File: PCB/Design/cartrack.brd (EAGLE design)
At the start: 100 x 80 mm, 37 parts, among them J1 POWER_JACKPTH, Q4 12MHz, Q5 LM2941, U1 ATMEGA644P-20AU

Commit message: Finished schematic.
Started on PCB.
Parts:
- removed J2: (no value), SparkFun-Connectors:JST-2-SMD
- removed JP1: USBSMD, SparkFun-Connectors:USB-MINIB
- removed U$3: SIMHOLDER, SparkFun-Connectors:SIMHOLDER
- added C10, C18: 1uF, SparkFun-Passives:CAP-PTH-SMALL
- added C12, C14, C19: 100nF, SparkFun-Passives:1206
- added C13, C6: (no value), SparkFun-Passives:0603-CAP
- added C15, C20: 10nF, SparkFun-Passives:0603-CAP
- added C7: 1mF, resistor:E3,5-8
- added C8, C9: 2.2uF, SparkFun-Passives:1206
- added L1, L2: (no value), resistor:L2012C
- added U$13: SIMHOLDER3, SparkFun-Connectors:SIMHOLDER3
- added X1: BU-SMA-V, con-coax:BU-SMA-V
- SJ1: value SOLDERJUMPERROUND -> SOLDERJUMPERNO; device SparkFun-Retired:SJ_ROUND -> SparkFun-Retired:SJ_2S-NO
- moved SPI 255.3 mm to (69.0, 19.0), turned to 270 degrees
- moved UARTS 246.6 mm to (46.0, 32.0), turned to 270 degrees
- moved JTAG 212.7 mm to (61.0, 51.0), turned to 90 degrees
- moved J1 206.5 mm to (48.0, -3.00)
- moved C5 203.5 mm to (37.0, 8.00), turned to 270 degrees
- moved C4 200.6 mm to (32.0, 16.0), turned to 90 degrees
- moved R13 184.8 mm to (35.4, 3.90), turned to 270 degrees
- moved R12 180.5 mm to (37.5, 3.90), turned to 270 degrees
- moved R11 177.1 mm to (43.5, 23.7), flipped to the bottom, turned to 270 degrees
- moved Q3 174.8 mm to (59.0, 43.0), flipped to the bottom
- moved S1 172.7 mm to (40.7, 17.6), turned to 270 degrees
- moved SJ1 172.3 mm to (60.0, 33.0), flipped to the bottom, turned to 180 degrees
- moved Q4 165.6 mm to (64.0, 10.0), flipped to the bottom
- moved R10 165.6 mm to (58.0, 39.0), flipped to the bottom, turned to 90 degrees
- moved R9 165.2 mm to (63.0, 41.0), flipped to the bottom, turned to 90 degrees
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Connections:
- new net ANT: C6.1, L2.1, U$1.RF_ANT
- new net N$14: C6.2, L1.1, X1.1
- net +2V8: now also C10.1, C12.1, C13.1, C14.1, C15.1
- net +4V: now also C18.1, C19.1, C20.1, C7.+, C8.1, C9.1
- net +5V: no longer J2.2, JP1.VBUS
- net 0V: now also C10.2, C12.2, C13.2, C14.2, C15.2, C18.2, C19.2, C20.2, C7.-, C8.2, C9.2, L1.2, L2.2, U$13.6, X1.2, X1.3, X1.4, X1.5; no longer J2.1, JP1.GND, U$3.C5
- net GSM_PWR: now also U$4.3
- net N$1: now also U$13.4, U$4.4; no longer U$3.C7, U$4.1
- net N$2: now also U$13.3, U$4.5; no longer U$3.C3, U$4.6
- net N$3: now also U$13.2, U$4.6; no longer U$3.C2, U$4.4
- net SIM_VDD: now also U$13.1, U$4.1; no longer U$3.C1, U$4.3
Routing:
- net +4V: track 0.00 -> 127.0 mm
- net +2V8: track 0.00 -> 87.9 mm, vias 0 -> 1
- net GSM_STATUS: track 0.00 -> 54.9 mm, vias 0 -> 3
- net NRESET: track 0.00 -> 52.4 mm
- net GSM_TX: track 0.00 -> 41.5 mm, vias 0 -> 2
- net GSM_PWR: track 0.00 -> 37.9 mm, vias 0 -> 1
- net GSM_RX: track 0.00 -> 36.5 mm, vias 0 -> 2
- net SIM_DATA: track 0.00 -> 33.0 mm, vias 0 -> 1
- net N$6: track 0.00 -> 31.9 mm
- net N$1: track 0.00 -> 28.1 mm
- net GPS_RESET: track 0.00 -> 28.0 mm, vias 0 -> 2
- net NETLIGHT: track 0.00 -> 25.9 mm, vias 0 -> 1
- net N$2: track 0.00 -> 23.0 mm
- net XTAL2: track 0.00 -> 21.4 mm
- net +5V: track 0.00 -> 19.6 mm
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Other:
- board size 100 x 80 mm -> 75 x 57 mm

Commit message: First draft of the PCB
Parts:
- moved R10 7.17 mm to (59.0, 46.1), turned to 180 degrees
- moved R9 3.31 mm to (62.8, 44.3), turned to 0 degrees
- moved C15 1.56 mm to (56.1, 32.1), turned to 90 degrees
- moved JTAG 1.00 mm to (62.0, 51.0)
- turned R8 to 270 degrees
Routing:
- net GPS_RX: track 14.9 -> 115.3 mm, vias 2 -> 4
- net +2V8: track 87.9 -> 155.0 mm, vias 1 -> 2
- net NRESET: track 52.4 -> 100.3 mm, vias 0 -> 1
- net TMS: track 0.00 -> 41.8 mm, vias 0 -> 1
- net TDI: track 0.00 -> 37.7 mm
- net TDO: track 0.00 -> 37.0 mm
- net TCK: track 0.00 -> 30.4 mm
- net ANT: track 0.00 -> 18.4 mm
- net GPS_TX: track 7.84 -> 24.8 mm, vias 0 -> 1
- net SIM_VDD: track 19.3 -> 32.8 mm, vias 0 -> 1
- net +4V: track 127.0 -> 138.2 mm
- net N$14: track 0.00 -> 9.15 mm
- net N$10: track 0.00 -> 8.45 mm, vias 0 -> 1
- net N$11: track 0.00 -> 6.05 mm
- net GPS_NRESET: track 0.00 -> 4.94 mm, vias 0 -> 1
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- added copper zone on layer 1, net 0V
- added copper zone on layer 16, net 0V

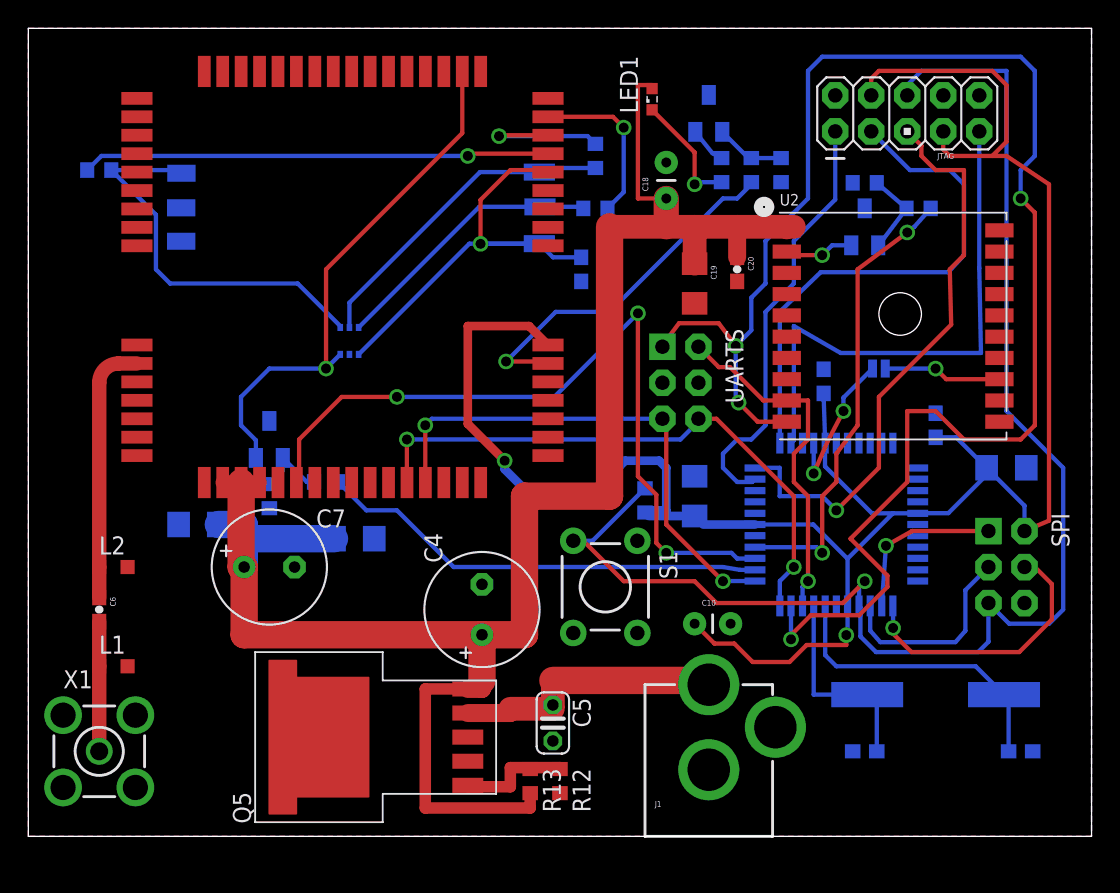
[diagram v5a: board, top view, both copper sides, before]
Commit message: Redone the PCB layout. Corrected mask and pad errors in the libraries
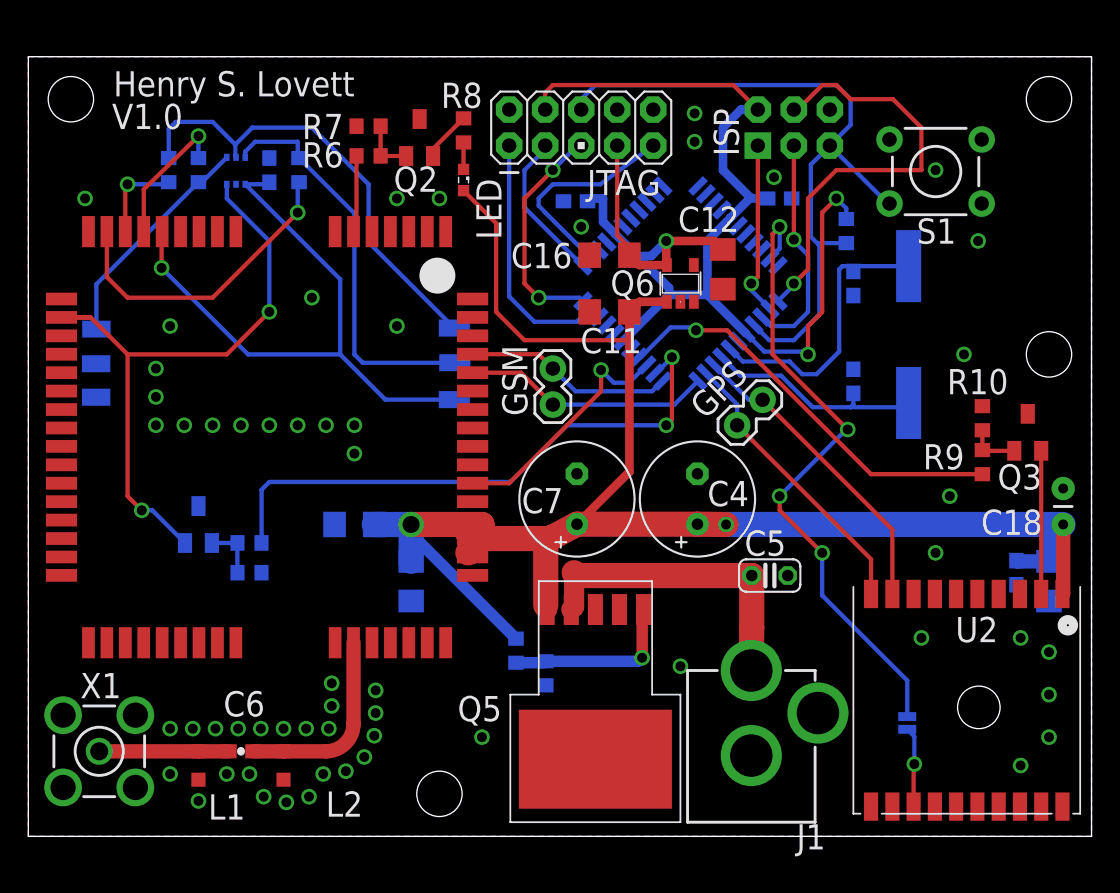
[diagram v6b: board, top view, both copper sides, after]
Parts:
- removed C10: 1uF, SparkFun-Passives:CAP-PTH-SMALL
- removed C14: 100nF, SparkFun-Passives:1206
- removed LED1: (no value), led:SML0603
- removed SPI, UARTS: (no value), SparkFun-Connectors:2X3-NS
- added C11: 1uF, SparkFun-Passives:1206
- added C16: 2.2uF, SparkFun-Passives:1206
- added GPS, GSM: M02PTH, SparkFun-Connectors:1X02
- added ISP: (no value), SparkFun-Connectors:2X3-NS
- added LED: (no value), led:SML0603
- added Q6: TPS70928, misc:SOT23-5
- moved S1 37.4 mm to (64.0, 46.9), turned to 0 degrees
- moved C18 36.2 mm to (73.0, 22.0)
- moved C2 35.0 mm to (58.2, 39.0), turned to 270 degrees
- moved C19 32.6 mm to (72.0, 18.0), flipped to the bottom
- moved R2 30.1 mm to (9.90, 47.0), turned to 90 degrees
- moved C13 29.9 mm to (38.6, 44.8), turned to 0 degrees
- moved R7 29.3 mm to (24.0, 50.1), flipped to the top, turned to 0 degrees
- moved C20 29.1 mm to (69.7, 18.6), flipped to the bottom
- moved R6 27.0 mm to (24.0, 48.0), flipped to the top, turned to 0 degrees
- moved U2 26.9 mm to (66.2, 9.60), turned to 270 degrees
- moved C3 26.1 mm to (58.2, 32.1), turned to 90 degrees
- moved Q4 25.5 mm to (62.1, 35.4), turned to 270 degrees
- moved SJ1 25.1 mm to (62.0, 8.00), turned to 270 degrees
- moved R11 23.7 mm to (57.7, 42.7), turned to 90 degrees
- moved C1 23.1 mm to (17.0, 47.0), turned to 90 degrees
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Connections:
- net N$1 renamed SIM_DATA_R
- net N$14 renamed ANT_1
- net N$2 renamed SIM_CLK_R
- net N$3 renamed SIM_RST_R
- removed net 0V: C1.2, C10.2, C12.2, C13.2, C14.2, C15.2, C18.2, C19.2, C2.2, C20.2, C3.2, C4.-, C5.2, C7.-, C8.2, C9.2, J1.GND, J1.GNDBREAK, JTAG.10, JTAG.2, L1.2, L2.2, Q1.3, Q2.3, Q3.3, Q5.GND, Q5.ONOFF, Q5.TAB, R10.1, R12.2, R5.1, R7.1, S1.1, SPI.6, U$1.AGND, U$1.GND1, U$1.GND2, U$1.GND3, U$1.GND4, U$1.GND5, U$1.GND6, U$1.GND7, U$1.GND8, U$13.6, U$4.2, U1.18, U1.28, U1.39, U1.6, U2.P$12, U2.P$19, U2.P$3, U2.P$8, UARTS.3, UARTS.4, X1.2, X1.3, X1.4, X1.5
- removed net PB4: U1.44
- new net GND: C1.2, C11.2, C12.2, C13.2, C15.2, C16.2, C18.2, C19.2, C2.2, C20.2, C3.2, C4.-, C5.2, C7.-, C8.2, C9.2, ISP.6, J1.GND, J1.GNDBREAK, JTAG.10, JTAG.2, L1.2, L2.2, Q1.3, Q2.3, Q3.3, Q5.GND, Q5.ONOFF, Q5.TAB, Q6.2, R10.1, R12.2, R5.1, R7.1, S1.1, U$1.AGND, U$1.GND1, U$1.GND2, U$1.GND3, U$1.GND4, U$1.GND5, U$1.GND6, U$1.GND7, U$1.GND8, U$13.6, U$4.2, U2.P$12, U2.P$19, U2.P$3, U2.P$8, X1.2, X1.3, X1.4, X1.5
- net +2V8: now also C16.1, ISP.2, Q6.5; no longer C10.1, C14.1, SPI.2, U$1.VDD_EXT
- net +4V: now also C11.1, LED.A, Q6.1; no longer LED1.A
- net GPS_RX: now also GPS.1; no longer UARTS.1
- net GPS_TX: now also GPS.2; no longer UARTS.2
- net GSM_RX: now also GSM.1; no longer UARTS.5
- net GSM_TX: now also GSM.2; no longer UARTS.6
- net N$10: now also LED.C; no longer LED1.C
- net N$13: now also U1.43; no longer U1.26
- net NRESET: now also ISP.5; no longer SPI.5
- net PB5: now also ISP.4; no longer SPI.4
- net PB6: now also ISP.1; no longer SPI.1
- net PB7: now also ISP.3; no longer SPI.3
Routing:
- net GPS_RX: track 115.3 -> 20.4 mm, vias 4 -> 0
- net +2V8: track 155.0 -> 95.2 mm, vias 2 -> 3
- net NRESET: track 100.3 -> 51.2 mm, vias 1 -> 0
- net GSM_STATUS: track 54.9 -> 17.4 mm, vias 3 -> 1
- net N$13: track 10.9 -> 45.2 mm, vias 2 -> 4
- net TDO: track 37.0 -> 10.8 mm
- net TMS: track 41.8 -> 16.6 mm, vias 1 -> 2
- net GSM_TX: track 41.5 -> 17.5 mm, vias 2 -> 0
- net SIM_DATA: track 33.0 -> 9.92 mm
- net TDI: track 37.7 -> 15.1 mm
- net GSM_RX: track 36.5 -> 14.8 mm, vias 2 -> 0
- net NETLIGHT: track 25.9 -> 5.43 mm, vias 1 -> 0
- net +4V: track 138.2 -> 122.3 mm, vias 0 -> 2
- net TCK: track 30.4 -> 17.5 mm
- net SIM_DATA_R: track 28.1 -> 16.1 mm
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- added copper zone on layer 1, net GND
- added copper zone on layer 16, net GND
- removed copper zone on layer 1, net 0V
- removed copper zone on layer 16, net 0V
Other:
- board size 75 x 57 mm -> 75 x 55 mm
- board text added: "Henry S. Lovett"
- board text added: "V1.0"
- board text added: "github.com/seblovett/cartrack"

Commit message: Some changes to the antenna
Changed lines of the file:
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@@
 <vertex x="0" y="0"/>
 </polygon>
-<polygon width="0.3048" layer="1">
+<polygon width="0.4064" layer="1">
 <vertex x="0" y="55"/>
 <vertex x="75" y="55"/>
 <vertex x="75" y="0"/>
-<vertex x="0" y="0"/>
+<vertex x="27" y="0"/>
+<vertex x="27" y="13"/>
+<vertex x="0" y="13"/>
 </polygon>
-<via x="10" y="7.6" extent="1-16" drill="0.7"/>
-<via x="11.6" y="7.6" extent="1-16" drill="0.7"/>
-<via x="13.2" y="7.6" extent="1-16" drill="0.7"/>
-<via x="14.8" y="7.6" extent="1-16" drill="0.7"/>
-<via x="16.4" y="7.6" extent="1-16" drill="0.7"/>
-<via x="18" y="7.6" extent="1-16" drill="0.7"/>
-<via x="19.6" y="7.6" extent="1-16" drill="0.7"/>
-<via x="21.2" y="7.6" extent="1-16" drill="0.7"/>
+<via x="10.05" y="8.1" extent="1-16" drill="0.7"/>
+<via x="11.65" y="8.1" extent="1-16" drill="0.7"/>
+<via x="13.2" y="8.1" extent="1-16" drill="0.7"/>
+<via x="14.8" y="8.1" extent="1-16" drill="0.7"/>
+<via x="16.4" y="8.1" extent="1-16" drill="0.7"/>
+<via x="18" y="8.1" extent="1-16" drill="0.7"/>
+<via x="19.6" y="8.1" extent="1-16" drill="0.7"/>
+<via x="29" y="10.9" extent="1-16" drill="0.7"/>
 <via x="39" y="43" extent="1-16" drill="0.7"/>
 <via x="52.6" y="46.5" extent="1-16" drill="0.7"/>
@@
 <via x="20" y="38" extent="1-16" drill="0.7"/>
 <via x="26" y="36" extent="1-16" drill="0.7"/>
-<via x="32" y="7" extent="1-16" drill="0.7"/>
+<via x="29" y="8" extent="1-16" drill="0.7"/>
 <via x="46" y="12" extent="1-16" drill="0.7"/>
 <via x="70" y="5" extent="1-16" drill="0.7"/>
@@
 <contactref element="R12" pad="2"/>
 <contactref element="C4" pad="-"/>
+<via x="10.1" y="3.8" extent="1-16" drill="0.7"/>
+<via x="12.9" y="2.3" extent="1-16" drill="0.7"/>
+<via x="14" y="3.8" extent="1-16" drill="0.7"/>
+<via x="16" y="3.8" extent="1-16" drill="0.7"/>
+<via x="16.7" y="2.4" extent="1-16" drill="0.7"/>
+<via x="19.3" y="2.4" extent="1-16" drill="0.7"/>
+<via x="20.7" y="3.8" extent="1-16" drill="0.7"/>
+<via x="22.3" y="3.9" extent="1-16" drill="0.7"/>
+<via x="23.9" y="4.4" extent="1-16" drill="0.7"/>
+<via x="24.9" y="6" extent="1-16" drill="0.7"/>
+<via x="25.2" y="9.2" extent="1-16" drill="0.7"/>
+<via x="25.2" y="7.6" extent="1-16" drill="0.7"/>
+<via x="25.2" y="10.8" extent="1-16" drill="0.7"/>
+<via x="20.7" y="10.8" extent="1-16" drill="0.7"/>
+<via x="20.7" y="9.3" extent="1-16" drill="0.7"/>
+<via x="11.3" y="2.3" extent="1-16" drill="0.7"/>
+<polygon width="0.3048" layer="1" isolate="0.6096">
+<vertex x="27" y="0"/>
+<vertex x="27" y="13"/>
+<vertex x="0" y="13"/>
+<vertex x="0" y="0"/>
+</polygon>
+<via x="32" y="8" extent="1-16" drill="0.7"/>
+<via x="32" y="11" extent="1-16" drill="0.7"/>
+<via x="17.7" y="10.8" extent="1-16" drill="0.7"/>
+<via x="13.7" y="10.8" extent="1-16" drill="0.7"/>
+<via x="10.7" y="10.8" extent="1-16" drill="0.7"/>
+<via x="7.7" y="10.8" extent="1-16" drill="0.7"/>
+<via x="4.7" y="10.8" extent="1-16" drill="0.7"/>
+<via x="56.3" y="24.4" extent="1-16" drill="0.7"/>
+<via x="53.4" y="27.3" extent="1-16" drill="0.7"/>
+<via x="31" y="40.4" extent="1-16" drill="0.7"/>
+<via x="2.5" y="48.2" extent="1-16" drill="0.7"/>
+<via x="24.2" y="52.8" extent="1-16" drill="0.7"/>
+<via x="64.5" y="51.5" extent="1-16" drill="0.7"/>
+<via x="34" y="27.6" extent="1-16" drill="0.7"/>
+<via x="34.2" y="29.7" extent="1-16" drill="0.7"/>
+<wire x1="47" y1="49" x2="52.6" y2="46.5" width="0" layer="19" extent="1-1"/>
 </signal>
 <signal name="+4V">
@@
 <contactref element="C6" pad="1"/>
 <contactref element="U$1" pad="RF_ANT"/>
-<wire x1="22.94" y1="13.66" x2="22.94" y2="7.94" width="1.016" layer="1"/>
-<wire x1="22.94" y1="7.94" x2="21" y2="6" width="1.016" layer="1" curve="-90"/>
-<wire x1="21" y1="6" x2="18" y2="6" width="1.016" layer="1"/>
-<wire x1="18" y1="6" x2="15.85" y2="6" width="1.016" layer="1"/>
+<wire x1="22.94" y1="13.66" x2="22.95" y2="13.66" width="1.27" layer="1"/>
+<wire x1="22.95" y1="13.66" x2="22.95" y2="12" width="1.27" layer="1"/>
+<wire x1="22.95" y1="12" x2="23" y2="11.85" width="1.4224" layer="1"/>
+<wire x1="23" y1="11.85" x2="23" y2="11" width="1.6764" layer="1"/>
+<wire x1="23" y1="11" x2="22.94" y2="7.94" width="1.7" layer="1"/>
+<wire x1="22.94" y1="7.94" x2="21" y2="6" width="1.7" layer="1" curve="-90"/>
+<wire x1="21" y1="6" x2="18" y2="6" width="1.7" layer="1"/>
+<wire x1="18" y1="6" x2="16" y2="6" width="1.7" layer="1"/>
+<wire x1="16" y1="6" x2="15.85" y2="6" width="1.4224" layer="1"/>
 </signal>
 <signal name="ANT_1">
@@
 <contactref element="L1" pad="1"/>
 <contactref element="X1" pad="1"/>
-<wire x1="14.15" y1="6" x2="12" y2="6" width="1.016" layer="1"/>
-<wire x1="12" y1="6" x2="5" y2="6" width="1.016" layer="1"/>
+<wire x1="14.15" y1="6" x2="13" y2="6" width="1.4224" layer="1"/>
+<wire x1="13" y1="6" x2="12" y2="6" width="1.7" layer="1"/>
+<wire x1="12" y1="6" x2="5" y2="6" width="1.7" layer="1"/>
 </signal>
 <signal name="AVCC">
@@
 <signal name="VCC_2">
 </signal>
-<signal name="N$1">
-<via x="21.4" y="9.2" extent="1-16" drill="0.7"/>
-</signal>
-<signal name="N$2">
-<via x="21.4" y="10.8" extent="1-16" drill="0.7"/>
-</signal>
-<signal name="N$3">
-<via x="10" y="4.4" extent="1-16" drill="0.7"/>
-</signal>
-<signal name="N$4">
-<via x="12" y="2.5" extent="1-16" drill="0.7"/>
-</signal>
-<signal name="N$12">
-<via x="14" y="4.4" extent="1-16" drill="0.7"/>
-</signal>
-<signal name="N$14">
-<via x="15.6" y="4.4" extent="1-16" drill="0.7"/>
-</signal>
-<signal name="N$15">
-<via x="16.6" y="2.8" extent="1-16" drill="0.7"/>
-</signal>
-<signal name="N$16">
-<via x="18.2" y="2.4" extent="1-16" drill="0.7"/>
-</signal>
-<signal name="N$17">
-<via x="19.8" y="2.8" extent="1-16" drill="0.7"/>
-</signal>
-<signal name="N$18">
-<via x="20.8" y="4.4" extent="1-16" drill="0.7"/>
-</signal>
-<signal name="N$19">
-<via x="22.4" y="4.6" extent="1-16" drill="0.7"/>
-</signal>
-<signal name="N$20">
-<via x="23.7" y="5.6" extent="1-16" drill="0.7"/>
-</signal>
-<signal name="N$21">
-<via x="24.4" y="7.1" extent="1-16" drill="0.7"/>
-</signal>
-<signal name="N$22">
-<via x="24.5" y="8.7" extent="1-16" drill="0.7"/>
-</signal>
-<signal name="N$23">
-<via x="24.5" y="10.3" extent="1-16" drill="0.7"/>
-</signal>
 <signal name="N$13">
